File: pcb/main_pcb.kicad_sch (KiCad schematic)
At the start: 18 parts, among them J1 Conn_01x06_Socket, SW1 SW_Push, SW2 SW_Push, U1 ESP32-H2-MINI-1, U2 LM5165Y

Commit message: Add JTAG header
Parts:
- added J2: Conn_01x10_Pin, Connector:Tag-Connect_TC2050-IDC-FP_2x05_P1.27mm_Vertical, symbol Connector:Conn_01x10_Pin
- C4: now not fitted
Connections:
- net +3.3V: now also J2.1 (Pin_1)
- net GND: now also J2.3 (Pin_3), J2.5 (Pin_5), J2.7 (Pin_7), J2.9 (Pin_9)
- net TCK: now reaches U1.18 (GPIO4/FSPICLK/ADC1_CH3/MTCK)
- net TCK: now also J2.4 (Pin_4)
- net TDI: now reaches U1.19 (GPIO5/FSPID/ADC1_CH4/MTDI)
- net TDI: now also J2.8 (Pin_8)
- net TMS: now reaches U1.5 (GPIO2/FSPIWP/ADC1_CH1/MTMS)
- net TMS: now also J2.2 (Pin_2)
- net TDO: now reaches U1.6 (GPIO3/FSPIHD/ADC1_CH2/MTDO)
- net TDO: now also J2.6 (Pin_6)
- no-connect marks 2 -> 3
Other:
- moved on the sheet: C5, C6, C7, C8, JP1, L1, R2, U2

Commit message: Add FTDI header
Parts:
- added J3: Conn_01x06_Pin, Connector_PinHeader_2.54mm:PinHeader_1x06_P2.54mm_Horizontal, symbol Connector:Conn_01x06_Pin
- added JP2: Jumper_2_Open, Connector_PinHeader_2.54mm:PinHeader_1x02_P2.54mm_Horizontal, symbol Jumper:Jumper_2_Open
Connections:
- net GND: now also J3.1 (Pin_1)
- net VDD: now also JP2.2 (B)
- net TXD: now reaches U1.30 (GPIO23/FSPICS1/U0RXD)
- net TXD: now also J3.4 (Pin_4)
- net RXD: now reaches U1.31 (GPIO24/FSPICS2/U0TXD)
- net RXD: now also J3.5 (Pin_5)
- new net: J3.3 (Pin_3), JP2.1 (A)
- no-connect marks 3 -> 5
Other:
- note added: "FTDI"
- moved on the sheet: D1
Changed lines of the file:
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@@
   (no_connect (at 35.56 153.67))
   (no_connect (at 68.58 102.87))
+  (no_connect (at 27.94 78.74))
+  (no_connect (at 27.94 88.9))
   (wire (pts (xy 52.07 38.1) (xy 52.07 35.56))
     (stroke (width 0) (type default))
@@
     (stroke (width 0) (type default))
   )
+  (wire (pts (xy 27.94 86.36) (xy 40.64 86.36))
+    (stroke (width 0) (type default))
+  )
   (wire (pts (xy 35.56 151.13) (xy 43.18 151.13))
     (stroke (width 0) (type default))
@@
     (stroke (width 0) (type default))
   )
+  (wire (pts (xy 193.04 59.69) (xy 207.01 59.69))
+    (stroke (width 0) (type default))
+  )
   (wire (pts (xy 193.04 80.01) (xy 207.01 80.01))
     (stroke (width 0) (type default))
   )
+  (wire (pts (xy 35.56 81.28) (xy 35.56 74.93))
+    (stroke (width 0) (type default))
+  )
   (wire (pts (xy 81.28 167.64) (xy 87.63 167.64))
     (stroke (width 0) (type default))
@@
     (stroke (width 0) (type default))
   )
+  (wire (pts (xy 27.94 76.2) (xy 33.02 76.2))
+    (stroke (width 0) (type default))
+  )
   (wire (pts (xy 146.05 160.02) (xy 144.78 160.02))
     (stroke (width 0) (type default))
@@
     (stroke (width 0) (type default))
   )
+  (wire (pts (xy 27.94 81.28) (xy 35.56 81.28))
+    (stroke (width 0) (type default))
+  )
+  (wire (pts (xy 35.56 62.23) (xy 35.56 64.77))
+    (stroke (width 0) (type default))
+  )
   (wire (pts (xy 35.56 146.05) (xy 43.18 146.05))
     (stroke (width 0) (type default))
@@
     (stroke (width 0) (type default))
   )
+  (wire (pts (xy 33.02 76.2) (xy 33.02 91.44))
+    (stroke (width 0) (type default))
+  )
   (wire (pts (xy 172.72 40.64) (xy 167.64 40.64))
     (stroke (width 0) (type default))
   )
+  (wire (pts (xy 27.94 83.82) (xy 40.64 83.82))
+    (stroke (width 0) (type default))
+  )
   (wire (pts (xy 68.58 97.79) (xy 76.2 97.79))
     (stroke (width 0) (type default))
@@
     (stroke (width 0) (type default))
   )
+  (wire (pts (xy 193.04 62.23) (xy 207.01 62.23))
+    (stroke (width 0) (type default))
+  )
   (wire (pts (xy 124.46 180.34) (xy 124.46 182.88))
     (stroke (width 0) (type default))
@@
     (stroke (width 0) (type default))
   )
+  (rectangle (start 15.24 55.88) (end 52.07 97.79)
+    (stroke (width 0) (type dash))
+    (fill (type none))
+  )
+  (text "FTDI" (at 15.24 55.88 0)
+    (effects (font (size 1.27 1.27)) (justify left bottom))
+  )
   (label "TMS" (at 52.07 133.35 0) (fields_autoplaced)
     (effects (font (size 1.27 1.27)) (justify left bottom))
@@
     (effects (font (size 1.27 1.27)) (justify left bottom))
   )
+  (label "RXD" (at 207.01 59.69 0) (fields_autoplaced)
+    (effects (font (size 1.27 1.27)) (justify left bottom))
+  )
   (label "TDI" (at 207.01 87.63 0) (fields_autoplaced)
     (effects (font (size 1.27 1.27)) (justify left bottom))
@@
     (effects (font (size 1.27 1.27)) (justify left bottom))
   )
+  (label "TXD" (at 207.01 62.23 0) (fields_autoplaced)
+    (effects (font (size 1.27 1.27)) (justify left bottom))
+  )
   (label "DATA_OUT" (at 76.2 105.41 0) (fields_autoplaced)
+    (effects (font (size 1.27 1.27)) (justify left bottom))
+  )
+  (label "RXD" (at 40.64 86.36 0) (fields_autoplaced)
+    (effects (font (size 1.27 1.27)) (justify left bottom))
+  )
+  (label "TXD" (at 40.64 83.82 0) (fields_autoplaced)
     (effects (font (size 1.27 1.27)) (justify left bottom))
   )
@@
     )
   )
+  (symbol (lib_id "Jumper:Jumper_2_Open") (at 35.56 69.85 90) (unit 1)
+    (in_bom yes) (on_board yes) (dnp no) (fields_autoplaced)
+    (property "Reference" "JP2" (at 36.83 68.58 90)
+      (effects (font (size 1.27 1.27)) (justify right))
+    )
+    (property "Value" "Jumper_2_Open" (at 36.83 71.12 90)
+      (effects (font (size 1.27 1.27)) (justify right))
+    )
+    (property "Footprint" "Connector_PinHeader_2.54mm:PinHeader_1x02_P2.54mm_Horizontal" (at 35.56 69.85 0)
+      (effects (font (size 1.27 1.27)) hide)
+    )
+    (property "Datasheet" "~" (at 35.56 69.85 0)
+      (effects (font (size 1.27 1.27)) hide)
+    )
+    (pin "2")
+    (pin "1")
+    (instances
+      (project "main_pcb"
+        (path "/6204b7c2-8814-41ee-9243-5078f55f08d4"
+          (reference "JP2") (unit 1)
+        )
+      )
+    )
+  )
   (symbol (lib_id "Device:R") (at 139.7 177.8 0) (unit 1)
     (in_bom yes) (on_board yes) (dnp no) (fields_autoplaced)
@@
     )
   )
+  (symbol (lib_id "power:VDD") (at 35.56 62.23 0) (unit 1)
+    (in_bom yes) (on_board yes) (dnp no)
+    (property "Reference" "#PWR020" (at 35.56 66.04 0)
+      (effects (font (size 1.27 1.27)) hide)
+    )
+    (property "Value" "VDD" (at 35.56 58.42 0)
+      (effects (font (size 1.27 1.27)))
+    )
+    (property "Footprint" "" (at 35.56 62.23 0)
+      (effects (font (size 1.27 1.27)) hide)
+    )
+    (property "Datasheet" "" (at 35.56 62.23 0)
+      (effects (font (size 1.27 1.27)) hide)
+    )
+    (pin "1")
+    (instances
+      (project "main_pcb"
+        (path "/6204b7c2-8814-41ee-9243-5078f55f08d4"
+          (reference "#PWR020") (unit 1)
+        )
+      )
+    )
+  )
   (symbol (lib_id "power:GND") (at 152.4 165.1 0) (unit 1)
     (in_bom yes) (on_board yes) (dnp no) (fields_autoplaced)
@@
     )
   )
+  (symbol (lib_id "power:GND") (at 33.02 91.44 0) (unit 1)
+    (in_bom yes) (on_board yes) (dnp no) (fields_autoplaced)
+    (property "Reference" "#PWR04" (at 33.02 97.79 0)
+      (effects (font (size 1.27 1.27)) hide)
+    )
+    (property "Value" "GND" (at 33.02 96.52 0)
+      (effects (font (size 1.27 1.27)))
+    )
+    (property "Footprint" "" (at 33.02 91.44 0)
+      (effects (font (size 1.27 1.27)) hide)
+    )
+    (property "Datasheet" "" (at 33.02 91.44 0)
+      (effects (font (size 1.27 1.27)) hide)
+    )
+    (pin "1")
+    (instances
+      (project "main_pcb"
+        (path "/6204b7c2-8814-41ee-9243-5078f55f08d4"
+          (reference "#PWR04") (unit 1)
+        )
+      )
+    )
+  )
   (symbol (lib_id "Switch:SW_Push") (at 97.79 99.06 90) (unit 1)
     (in_bom yes) (on_board yes) (dnp no) (fields_autoplaced)
@@
     )
   )
-  (symbol (lib_id "Device:LED_RAGB") (at 45.72 78.74 0) (unit 1)
-    (in_bom yes) (on_board yes) (dnp no) (fields_autoplaced)
-    (property "Reference" "D1" (at 45.72 66.04 0)
-      (effects (font (size 1.27 1.27)))
-    )
-    (property "Value" "LED_RAGB" (at 45.72 68.58 0)
-      (effects (font (size 1.27 1.27)))
-    )
-    (property "Footprint" "LED_SMD:LED_RGB_1210" (at 45.72 80.01 0)
-      (effects (font (size 1.27 1.27)) hide)
-    )
-    (property "Datasheet" "~" (at 45.72 80.01 0)
+  (symbol (lib_id "Device:LED_RAGB") (at 200.66 123.19 0) (unit 1)
+    (in_bom yes) (on_board yes) (dnp no) (fields_autoplaced)
+    (property "Reference" "D1" (at 200.66 110.49 0)
+      (effects (font (size 1.27 1.27)))
+    )
+    (property "Value" "LED_RAGB" (at 200.66 113.03 0)
+      (effects (font (size 1.27 1.27)))
+    )
+    (property "Footprint" "LED_SMD:LED_RGB_1210" (at 200.66 124.46 0)
+      (effects (font (size 1.27 1.27)) hide)
+    )
+    (property "Datasheet" "~" (at 200.66 124.46 0)
       (effects (font (size 1.27 1.27)) hide)
     )
@@
         )
       )
+    )
+  )
+  (symbol (lib_id "Connector:Conn_01x06_Pin") (at 22.86 81.28 0) (unit 1)
+    (in_bom yes) (on_board yes) (dnp no) (fields_autoplaced)
+    (property "Reference" "J3" (at 23.495 71.12 0)
+      (effects (font (size 1.27 1.27)))
+    )
+    (property "Value" "Conn_01x06_Pin" (at 23.495 73.66 0)
+      (effects (font (size 1.27 1.27)))
+    )
+    (property "Footprint" "Connector_PinHeader_2.54mm:PinHeader_1x06_P2.54mm_Horizontal" (at 22.86 81.28 0)
+      (effects (font (size 1.27 1.27)) hide)
+    )
+    (property "Datasheet" "~" (at 22.86 81.28 0)
+      (effects (font (size 1.27 1.27)) hide)
+    )
+    (pin "2")
+    (pin "3")
+    (pin "4")
+    (pin "5")
+    (pin "6")
+    (pin "1")
+    (instances
+      (project "main_pcb"
+        (path "/6204b7c2-8814-41ee-9243-5078f55f08d4"
+          (reference "J3") (unit 1)
+        )
+      )

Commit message: Add optional soft start capacitor to power circuit
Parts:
- added C9: 1uF, Capacitor_SMD:C_1206_3216Metric_Pad1.33x1.80mm_HandSolder, symbol Device:C
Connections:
- net GND: now also C9.2
- net at U2.4 (SS): now also C9.1
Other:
- note added: "JTAG"
- note added: "Power"
- moved on the sheet: C5, C6, C7, C8, J2, JP1, L1, R2, SW1, U2

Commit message: Add USB-C receptacle
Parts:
- added J4: USB_C_Receptacle_USB2.0, Connector_USB:USB_C_Receptacle_HRO_TYPE-C-31-M-12, symbol Connector:USB_C_Receptacle_USB2.0
- added JP3: SolderJumper_2_Bridged, Jumper:SolderJumper-2_P1.3mm_Open_TrianglePad1.0x1.5mm, symbol Jumper:SolderJumper_2_Bridged
- added R3, R4: 5k1, Resistor_SMD:R_1206_3216Metric_Pad1.30x1.75mm_HandSolder, symbol Device:R
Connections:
- net GND: now also J4.A1 (GND), J4.A12 (GND), J4.B1 (GND), J4.B12 (GND), R3.2, R4.2
- net VDD: now also JP3.2 (B)
- net D-: now reaches U1.26 (GPIO26/FSPICS4/USB_D-)
- net D-: now also J4.A7 (D-), J4.B7 (D-)
- net D+: now reaches U1.27 (GPIO27/FSPICS5/USB_D+)
- net D+: now also J4.A6 (D+), J4.B6 (D+)
- new net: J4.B5 (CC2), R4.1
- new net: J4.A5 (CC1), R3.1
- new net: J4.A4 (VBUS), J4.A9 (VBUS), J4.B4 (VBUS), J4.B9 (VBUS), JP3.1 (A)
- no-connect marks 5 -> 8
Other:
- note added: "RESET"
- note added: "USB"
- moved on the sheet: C3, C4, C5, C6, C7, C8, C9, J1, J2, J3, JP1, JP2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

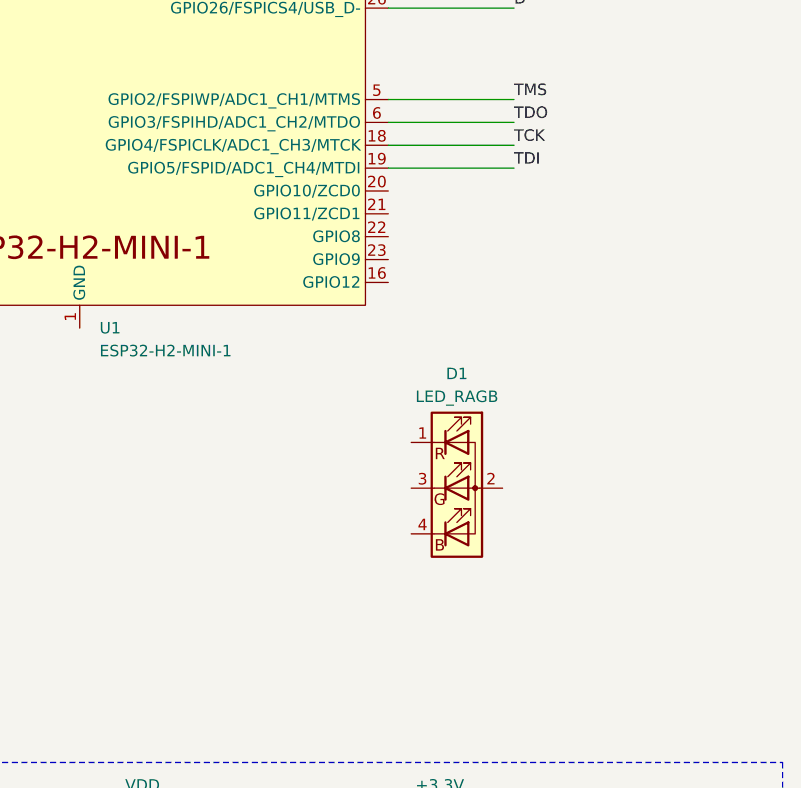
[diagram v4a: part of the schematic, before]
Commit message: Add boot selection circuit
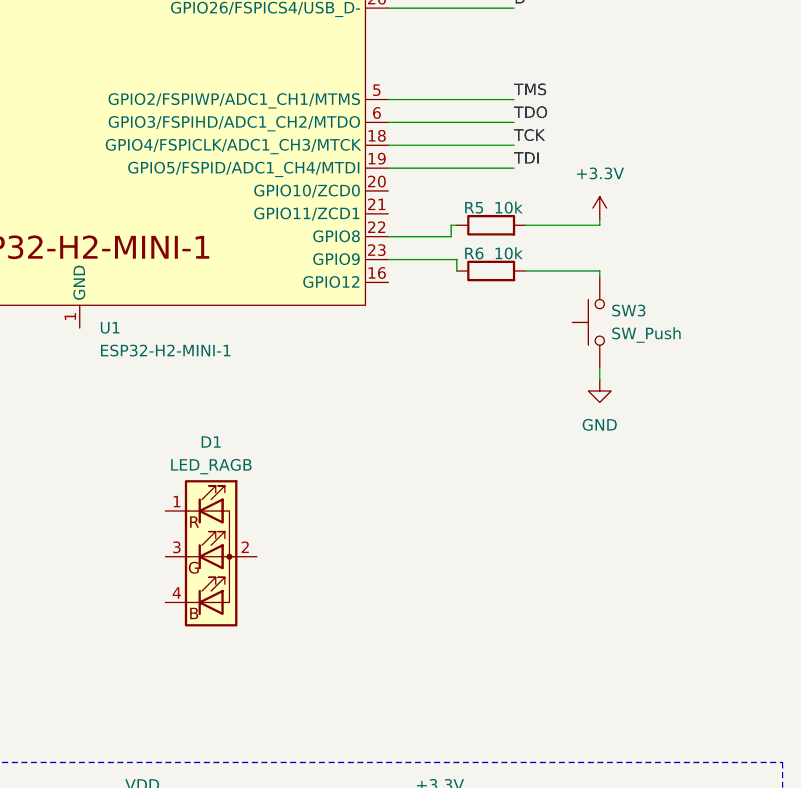
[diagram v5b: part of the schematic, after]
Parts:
- added R5, R6: 10k, Resistor_SMD:R_1206_3216Metric_Pad1.30x1.75mm_HandSolder, symbol Device:R
- added SW3: SW_Push, Button_Switch_SMD:SW_SPST_PTS645, symbol Switch:SW_Push
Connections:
- net +3.3V: now also R5.2
- net GND: now also SW3.1
- net at U1.22 (GPIO8): now also R5.1
- net at U1.23 (GPIO9): now also R6.1
- new net: R6.2, SW3.2
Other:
- moved on the sheet: D1
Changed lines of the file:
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@@
+    (stroke (width 0) (type default))
+  )
+  (wire (pts (xy 200.025 93.98) (xy 200.025 95.25))
     (stroke (width 0) (type default))
   )
@@
     (stroke (width 0) (type default))
   )
+  (wire (pts (xy 216.535 93.345) (xy 216.535 93.98))
+    (stroke (width 0) (type default))
+  )
   (wire (pts (xy 202.565 189.23) (xy 202.565 187.96))
     (stroke (width 0) (type default))
   )
+  (wire (pts (xy 216.535 99.695) (xy 216.535 99.06))
+    (stroke (width 0) (type default))
+  )
   (wire (pts (xy 29.845 153.035) (xy 34.925 153.035))
     (stroke (width 0) (type default))
@@
     (stroke (width 0) (type default))
   )
+  (wire (pts (xy 216.535 109.855) (xy 216.535 111.125))
+    (stroke (width 0) (type default))
+  )
   (wire (pts (xy 162.56 40.64) (xy 167.64 40.64))
     (stroke (width 0) (type default))
@@
     (stroke (width 0) (type default))
   )
+  (wire (pts (xy 193.04 97.79) (xy 200.66 97.79))
+    (stroke (width 0) (type default))
+  )
   (wire (pts (xy 198.755 180.34) (xy 220.345 180.34))
     (stroke (width 0) (type default))
@@
     (stroke (width 0) (type default))
   )
+  (wire (pts (xy 216.535 99.06) (xy 208.28 99.06))
+    (stroke (width 0) (type default))
+  )
   (wire (pts (xy 29.845 241.935) (xy 37.465 241.935))
     (stroke (width 0) (type default))
@@
     (stroke (width 0) (type default))
   )
+  (wire (pts (xy 216.535 93.98) (xy 208.28 93.98))
+    (stroke (width 0) (type default))
+  )
   (wire (pts (xy 37.465 236.855) (xy 37.465 229.235))
     (stroke (width 0) (type default))
@@
     (stroke (width 0) (type default))
   )
+  (wire (pts (xy 200.66 97.79) (xy 200.66 99.06))
+    (stroke (width 0) (type default))
+  )
   (wire (pts (xy 174.625 195.58) (xy 174.625 198.12))
     (stroke (width 0) (type default))
@@
     (stroke (width 0) (type default))
   )
+  (wire (pts (xy 200.025 93.98) (xy 200.66 93.98))
+    (stroke (width 0) (type default))
+  )
   (wire (pts (xy 202.565 187.96) (xy 192.405 187.96))
     (stroke (width 0) (type default))
@@
   )
   (wire (pts (xy 34.925 141.605) (xy 34.925 140.335))
+    (stroke (width 0) (type default))
+  )
+  (wire (pts (xy 200.025 95.25) (xy 193.04 95.25))
     (stroke (width 0) (type default))
   )
@@
     )
   )
+  (symbol (lib_id "Device:R") (at 204.47 93.98 90) (unit 1)
+    (in_bom yes) (on_board yes) (dnp no)
+    (property "Reference" "R5" (at 202.565 92.075 90)
+      (effects (font (size 1.27 1.27)))
+    )
+    (property "Value" "10k" (at 206.375 92.075 90)
+      (effects (font (size 1.27 1.27)))
+    )
+    (property "Footprint" "Resistor_SMD:R_1206_3216Metric_Pad1.30x1.75mm_HandSolder" (at 204.47 95.758 90)
+      (effects (font (size 1.27 1.27)) hide)
+    )
+    (property "Datasheet" "~" (at 204.47 93.98 0)
+      (effects (font (size 1.27 1.27)) hide)
+    )
+    (pin "2")
+    (pin "1")
+    (instances
+      (project "main_pcb"
+        (path "/6204b7c2-8814-41ee-9243-5078f55f08d4"
+          (reference "R5") (unit 1)
+        )
+      )
+    )
+  )
   (symbol (lib_id "Device:R") (at 192.405 193.04 0) (unit 1)
     (in_bom yes) (on_board yes) (dnp no) (fields_autoplaced)
@@
         (path "/6204b7c2-8814-41ee-9243-5078f55f08d4"
           (reference "R2") (unit 1)
+        )
+      )
+    )
+  )
+  (symbol (lib_id "Switch:SW_Push") (at 216.535 104.775 90) (unit 1)
+    (in_bom yes) (on_board yes) (dnp no) (fields_autoplaced)
+    (property "Reference" "SW3" (at 217.805 103.505 90)
+      (effects (font (size 1.27 1.27)) (justify right))
+    )
+    (property "Value" "SW_Push" (at 217.805 106.045 90)
+      (effects (font (size 1.27 1.27)) (justify right))
+    )
+    (property "Footprint" "Button_Switch_SMD:SW_SPST_PTS645" (at 211.455 104.775 0)
+      (effects (font (size 1.27 1.27)) hide)
+    )
+    (property "Datasheet" "~" (at 211.455 104.775 0)
+      (effects (font (size 1.27 1.27)) hide)
+    )
+    (pin "2")
+    (pin "1")
+    (instances
+      (project "main_pcb"
+        (path "/6204b7c2-8814-41ee-9243-5078f55f08d4"
+          (reference "SW3") (unit 1)
         )
       )
@@
     )
   )
+  (symbol (lib_id "Device:R") (at 204.47 99.06 90) (unit 1)
+    (in_bom yes) (on_board yes) (dnp no)
+    (property "Reference" "R6" (at 202.565 97.155 90)
+      (effects (font (size 1.27 1.27)))
+    )
+    (property "Value" "10k" (at 206.375 97.155 90)
+      (effects (font (size 1.27 1.27)))
+    )
+    (property "Footprint" "Resistor_SMD:R_1206_3216Metric_Pad1.30x1.75mm_HandSolder" (at 204.47 100.838 90)
+      (effects (font (size 1.27 1.27)) hide)
+    )
+    (property "Datasheet" "~" (at 204.47 99.06 0)
+      (effects (font (size 1.27 1.27)) hide)
+    )
+    (pin "2")
+    (pin "1")
+    (instances
+      (project "main_pcb"
+        (path "/6204b7c2-8814-41ee-9243-5078f55f08d4"
+          (reference "R6") (unit 1)
+        )
+      )
+    )
+  )
   (symbol (lib_id "power:+3.3V") (at 37.465 229.235 0) (unit 1)
     (in_bom yes) (on_board yes) (dnp no) (fields_autoplaced)
@@
         (path "/6204b7c2-8814-41ee-9243-5078f55f08d4"
           (reference "#PWR011") (unit 1)
+        )
+      )
+    )
+  )
+  (symbol (lib_id "power:+3.3V") (at 216.535 93.345 0) (unit 1)
+    (in_bom yes) (on_board yes) (dnp no) (fields_autoplaced)
+    (property "Reference" "#PWR025" (at 216.535 97.155 0)
+      (effects (font (size 1.27 1.27)) hide)
+    )
+    (property "Value" "+3.3V" (at 216.535 88.265 0)
+      (effects (font (size 1.27 1.27)))
+    )
+    (property "Footprint" "" (at 216.535 93.345 0)
+      (effects (font (size 1.27 1.27)) hide)
+    )
+    (property "Datasheet" "" (at 216.535 93.345 0)
+      (effects (font (size 1.27 1.27)) hide)
+    )
+    (pin "1")
+    (instances
+      (project "main_pcb"
+        (path "/6204b7c2-8814-41ee-9243-5078f55f08d4"
+          (reference "#PWR025") (unit 1)
         )
       )
@@
     )
   )
+  (symbol (lib_id "power:GND") (at 216.535 111.125 0) (unit 1)
+    (in_bom yes) (on_board yes) (dnp no) (fields_autoplaced)
+    (property "Reference" "#PWR026" (at 216.535 117.475 0)
+      (effects (font (size 1.27 1.27)) hide)
+    )
+    (property "Value" "GND" (at 216.535 116.205 0)
+      (effects (font (size 1.27 1.27)))
+    )
+    (property "Footprint" "" (at 216.535 111.125 0)
+      (effects (font (size 1.27 1.27)) hide)
+    )
+    (property "Datasheet" "" (at 216.535 111.125 0)
+      (effects (font (size 1.27 1.27)) hide)
+    )
+    (pin "1")
+    (instances
+      (project "main_pcb"
+        (path "/6204b7c2-8814-41ee-9243-5078f55f08d4"
+          (reference "#PWR026") (unit 1)
+        )
+      )
+    )
+  )
   (symbol (lib_id "power:GND") (at 86.995 222.885 0) (unit 1)
     (in_bom yes) (on_board yes) (dnp no) (fields_autoplaced)
@@
     )
   )
-  (symbol (lib_id "Device:LED_RAGB") (at 200.66 123.19 0) (unit 1)
-    (in_bom yes) (on_board yes) (dnp no) (fields_autoplaced)
-    (property "Reference" "D1" (at 200.66 110.49 0)
-      (effects (font (size 1.27 1.27)))
-    )
-    (property "Value" "LED_RAGB" (at 200.66 113.03 0)
-      (effects (font (size 1.27 1.27)))
-    )
-    (property "Footprint" "LED_SMD:LED_RGB_1210" (at 200.66 124.46 0)
-      (effects (font (size 1.27 1.27)) hide)
-    )
-    (property "Datasheet" "~" (at 200.66 124.46 0)
-      (effects (font (size 1.27 1.27)) hide)
-    )
+  (symbol (lib_id "Device:LED_RAGB") (at 173.355 130.81 0) (unit 1)
+    (in_bom yes) (on_board yes) (dnp no) (fields_autoplaced)
+    (property "Reference" "D1" (at 173.355 118.11 0)
+      (effects (font (size 1.27 1.27)))
+    )
+    (property "Value" "LED_RAGB" (at 173.355 120.65 0)
+      (effects (font (size 1.27 1.27)))
+    )
+    (property "Footprint" "LED_SMD:LED_RGB_1210" (at 173.355 132.08 0)
+      (effects (font (size 1.27 1.27)) hide)
+    )
+    (property "Datasheet" "~" (at 173.355 132.08 0)
+      (effects (font (size 1.27 1.27)) hide)
+    )
